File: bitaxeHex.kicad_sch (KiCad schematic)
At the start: 21 parts, among them J1 Screw Terminal, J2 Screw Terminal

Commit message: Move USB-C connector away from ESP32 to make room for chunky cables
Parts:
- J1, J2: footprint bitaxe:7770-screw-terminal -> bitaxe:7771-screw-terminal; DK 36-7770-ND -> 36-7771-ND; PARTNO 36-7770 -> 36-7771
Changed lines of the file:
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@@
       (effects (font (size 1.27 1.27)) hide)
     )
-    (property "Footprint" "bitaxe:7770-screw-terminal" (at 32.385 33.02 0)
+    (property "Footprint" "bitaxe:7771-screw-terminal" (at 32.385 33.02 0)
       (effects (font (size 1.27 1.27)) hide)
     )
@@
       (effects (font (size 1.27 1.27)) hide)
     )
-    (property "DK" "36-7770-ND" (at 32.385 33.02 0)
-      (effects (font (size 1.27 1.27)) hide)
-    )
-    (property "PARTNO" "36-7770" (at 32.385 33.02 0)
+    (property "DK" "36-7771-ND" (at 32.385 33.02 0)
+      (effects (font (size 1.27 1.27)) hide)
+    )
+    (property "PARTNO" "36-7771" (at 32.385 33.02 0)
       (effects (font (size 1.27 1.27)) hide)
     )
@@
       (effects (font (size 1.27 1.27)) hide)
     )
-    (property "Footprint" "bitaxe:7770-screw-terminal" (at 32.385 40.64 0)
-      (effects (font (size 1.27 1.27)) hide)
-    )
-    (property "Datasheet" "https://www.te.com/commerce/DocumentDelivery/DDEController?Action=srchrtrv&DocNm=63862&DocType=Customer+Drawing&DocLang=English" (at 32.385 40.64 0)
-      (effects (font (size 1.27 1.27)) hide)
-    )
-    (property "DK" "36-7770-ND" (at 32.385 40.64 0)
-      (effects (font (size 1.27 1.27)) hide)
-    )
-    (property "PARTNO" "36-7770" (at 32.385 40.64 0)
-      (effects (font (size 1.27 1.27)) hide)
-    )
+    (property "Footprint" "bitaxe:7771-screw-terminal" (at 32.385 40.64 0)
+      (effects (font (size 1.27 1.27)) hide)
+    )
+    (property "Datasheet" "https://mm.digikey.com/Volume0/opasdata/d220001/medias/docus/581/Metric_PCB_Screw_Terminals.pdf" (at 32.385 40.64 0)
+      (effects (font (size 1.27 1.27)) hide)
+    )
+    (property "DK" "36-7771-ND" (at 32.385 40.64 0)
+      (effects (font (size 1.27 1.27)) hide)
+    )
+    (property "PARTNO" "36-7771" (at 32.385 40.64 0)
+      (effects (font (size 1.27 1.27)) hide)
+    )

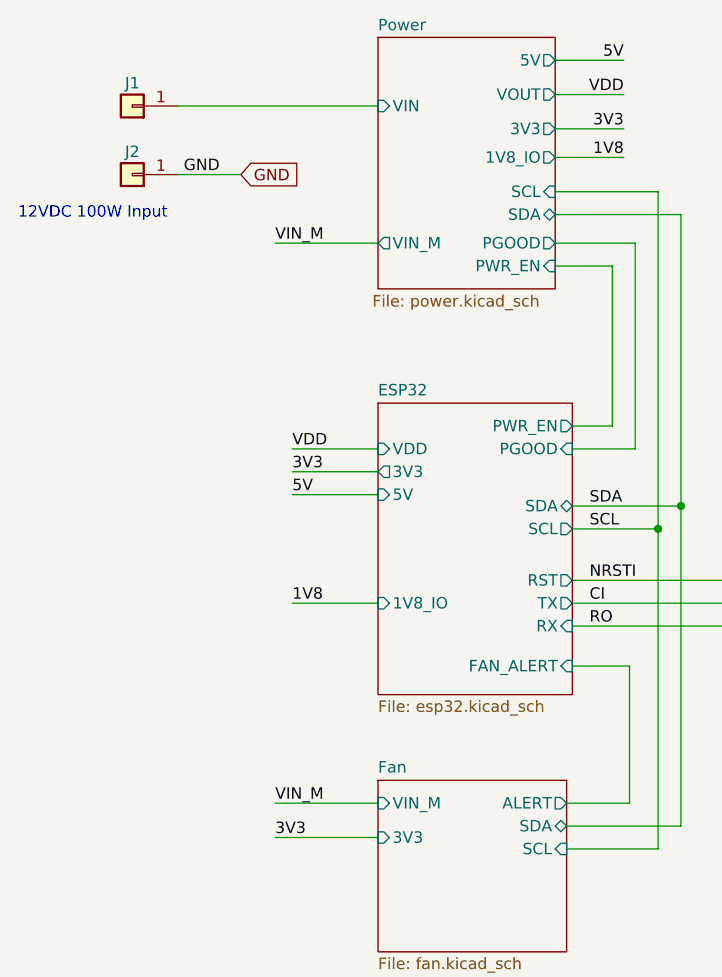
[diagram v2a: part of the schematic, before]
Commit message: remove INA219 power monitor
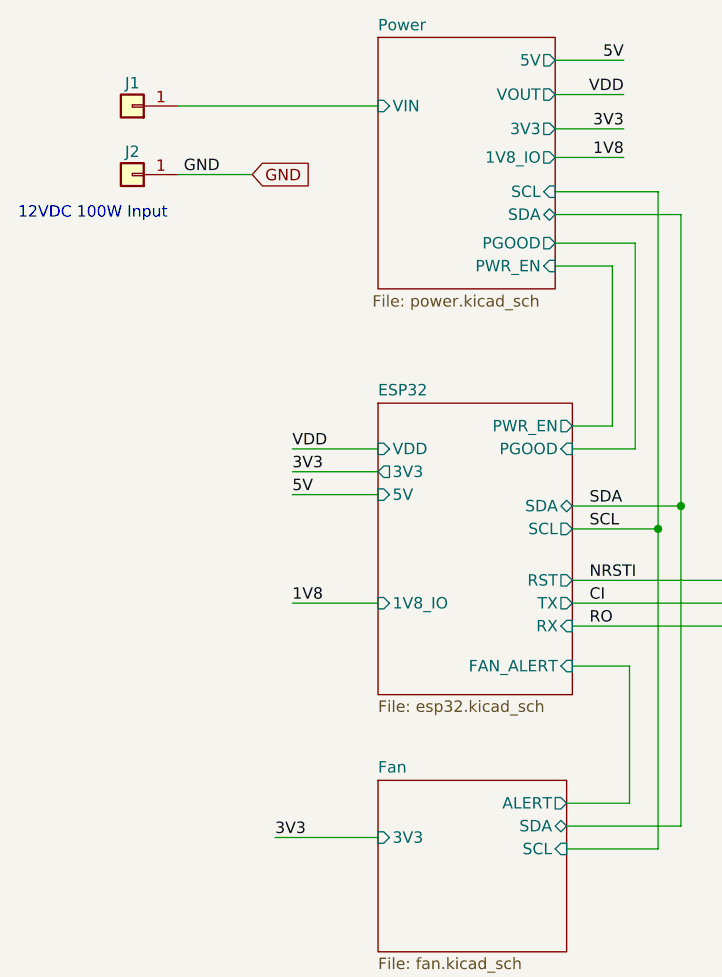
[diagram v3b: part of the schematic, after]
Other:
- sheet Fan ports: added none; removed VIN_M
- sheet Power ports: added none; removed VIN_M
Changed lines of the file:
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@@
-    (stroke (width 0) (type default))
-  )
-  (wire (pts (xy 48.26 110.49) (xy 59.69 110.49))
     (stroke (width 0) (type default))
   )
@@
     (stroke (width 0) (type default))
   )
-  (wire (pts (xy 37.465 40.64) (xy 44.45 40.64))
-    (stroke (width 0) (type default))
-  )
   (wire (pts (xy 200.66 76.2) (xy 191.77 76.2))
     (stroke (width 0) (type default))
@@
     (stroke (width 0) (type default))
   )
-  (wire (pts (xy 48.26 48.26) (xy 59.69 48.26))
-    (stroke (width 0) (type default))
-  )
   (wire (pts (xy 81.28 88.265) (xy 123.825 88.265))
     (stroke (width 0) (type default))
@@
   )
   (wire (pts (xy 93.345 113.03) (xy 93.345 77.47))
+    (stroke (width 0) (type default))
+  )
+  (wire (pts (xy 37.465 40.64) (xy 45.72 40.64))
     (stroke (width 0) (type default))
   )
@@
     (effects (font (size 1.27 1.27)) (justify left bottom))
   )
-  (label "VIN_M" (at 48.26 48.26 0) (fields_autoplaced)
-    (effects (font (size 1.27 1.27)) (justify left bottom))
-  )
   (label "GND" (at 106.68 114.935 0) (fields_autoplaced)
     (effects (font (size 1.27 1.27)) (justify left bottom))
@@
     (effects (font (size 1.27 1.27)) (justify left bottom))
   )
-  (label "VIN_M" (at 48.26 110.49 0) (fields_autoplaced)
-    (effects (font (size 1.27 1.27)) (justify left bottom))
-  )
   (label "SCL" (at 83.185 80.01 0) (fields_autoplaced)
     (effects (font (size 1.27 1.27)) (justify left bottom))
@@
     (effects (font (size 1.27 1.27)) (justify right bottom))
   )
-  (global_label "GND" (shape input) (at 44.45 40.64 0) (fields_autoplaced)
+  (global_label "GND" (shape input) (at 45.72 40.64 0) (fields_autoplaced)
     (effects (font (size 1.27 1.27)) (justify left))
-    (property "Intersheetrefs" "${INTERSHEET_REFS}" (at 50.7336 40.5606 0)
+    (property "Intersheetrefs" "${INTERSHEET_REFS}" (at 52.0036 40.5606 0)
       (effects (font (size 1.27 1.27)) (justify left) hide)
     )
@@
       (effects (font (size 1.27 1.27)) (justify right))
     )
-    (pin "VIN_M" input (at 59.69 110.49 180)
-      (effects (font (size 1.27 1.27)) (justify left))
-    )
     (instances
       (project "bitaxeHex"
@@
       (effects (font (size 1.27 1.27)) (justify right))
     )
-    (pin "VIN_M" output (at 59.69 48.26 180)
-      (effects (font (size 1.27 1.27)) (justify left))
-    )
-    (instances
+    (instances

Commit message: more routing
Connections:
- net Power/VIN renamed VIN
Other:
- sheet ESP32 ports: added SMB_ALRT; removed none
- sheet Fan ports: added 5V, VIN; removed none
- sheet Power ports: added GND, SMB_ALRT; removed none
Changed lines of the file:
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@@
+    (stroke (width 0) (type default))
+  )
+  (wire (pts (xy 96.52 40.005) (xy 79.375 40.005))
+    (stroke (width 0) (type default))
+  )
+  (wire (pts (xy 81.28 74.93) (xy 96.52 74.93))
     (stroke (width 0) (type default))
   )
@@
     (stroke (width 0) (type default))
   )
+  (wire (pts (xy 48.26 111.76) (xy 59.69 111.76))
+    (stroke (width 0) (type default))
+  )
   (wire (pts (xy 154.94 76.2) (xy 154.94 68.58))
     (stroke (width 0) (type default))
@@
     (stroke (width 0) (type default))
   )
-  (wire (pts (xy 79.375 38.735) (xy 86.995 38.735))
+  (wire (pts (xy 79.375 36.195) (xy 86.995 36.195))
+    (stroke (width 0) (type default))
+  )
+  (wire (pts (xy 48.895 48.895) (xy 59.69 48.895))
     (stroke (width 0) (type default))
   )
@@
     (stroke (width 0) (type default))
   )
+  (wire (pts (xy 96.52 74.93) (xy 96.52 40.005))
+    (stroke (width 0) (type default))
+  )
   (wire (pts (xy 179.07 90.805) (xy 200.66 90.805))
     (stroke (width 0) (type default))
@@
     (stroke (width 0) (type default))
   )
-  (wire (pts (xy 48.26 114.3) (xy 59.69 114.3))
+  (wire (pts (xy 48.26 116.84) (xy 59.69 116.84))
     (stroke (width 0) (type default))
   )
@@
     (stroke (width 0) (type default))
   )
+  (wire (pts (xy 48.26 123.19) (xy 59.69 123.19))
+    (stroke (width 0) (type default))
+  )
   (wire (pts (xy 154.94 99.06) (xy 161.29 99.06))
     (stroke (width 0) (type default))
@@
     (stroke (width 0) (type default))
   )
-  (wire (pts (xy 79.375 31.75) (xy 86.995 31.75))
+  (wire (pts (xy 79.375 29.21) (xy 86.995 29.21))
     (stroke (width 0) (type default))
   )
@@
     (stroke (width 0) (type default))
   )
-  (wire (pts (xy 79.375 27.94) (xy 86.995 27.94))
+  (wire (pts (xy 79.375 25.4) (xy 86.995 25.4))
     (stroke (width 0) (type default))
   )
@@
     (stroke (width 0) (type default))
   )
-  (wire (pts (xy 79.375 35.56) (xy 86.995 35.56))
+  (wire (pts (xy 79.375 33.02) (xy 86.995 33.02))
     (stroke (width 0) (type default))
   )
@@
     (effects (font (size 1.27 1.27)) (justify left bottom))
   )
+  (label "SMB_ALRT" (at 85.09 40.005 0) (fields_autoplaced)
+    (effects (font (size 1.27 1.27)) (justify left bottom))
+  )
   (label "1V8" (at 50.165 88.265 0) (fields_autoplaced)
     (effects (font (size 1.27 1.27)) (justify left bottom))
   )
-  (label "5V" (at 86.995 27.94 180) (fields_autoplaced)
+  (label "5V" (at 86.995 25.4 180) (fields_autoplaced)
     (effects (font (size 1.27 1.27)) (justify right bottom))
   )
@@
     (effects (font (size 1.27 1.27)) (justify right bottom))
   )
+  (label "5V" (at 48.26 123.19 0) (fields_autoplaced)
+    (effects (font (size 1.27 1.27)) (justify left bottom))
+  )
   (label "CI" (at 83.185 88.265 0) (fields_autoplaced)
     (effects (font (size 1.27 1.27)) (justify left bottom))
@@
     (effects (font (size 1.27 1.27)) (justify left bottom))
   )
-  (label "1V8" (at 86.995 38.735 180) (fields_autoplaced)
+  (label "1V8" (at 86.995 36.195 180) (fields_autoplaced)
     (effects (font (size 1.27 1.27)) (justify right bottom))
   )
-  (label "3V3" (at 86.995 35.56 180) (fields_autoplaced)
+  (label "VIN" (at 48.26 111.76 0) (fields_autoplaced)
+    (effects (font (size 1.27 1.27)) (justify left bottom))
+  )
+  (label "3V3" (at 86.995 33.02 180) (fields_autoplaced)
     (effects (font (size 1.27 1.27)) (justify right bottom))
   )
@@
     (effects (font (size 1.27 1.27)) (justify left bottom))
   )
-  (label "3V3" (at 48.26 114.3 0) (fields_autoplaced)
+  (label "3V3" (at 48.26 116.84 0) (fields_autoplaced)
     (effects (font (size 1.27 1.27)) (justify left bottom))
   )
@@
     (effects (font (size 1.27 1.27)) (justify left bottom))
   )
-  (label "VDD" (at 86.995 31.75 180) (fields_autoplaced)
+  (label "VDD" (at 86.995 29.21 180) (fields_autoplaced)
     (effects (font (size 1.27 1.27)) (justify right bottom))
+  )
+  (label "GND" (at 48.895 48.895 0) (fields_autoplaced)
+    (effects (font (size 1.27 1.27)) (justify left bottom))
+  )
+  (label "VIN" (at 47.625 33.02 0) (fields_autoplaced)
+    (effects (font (size 1.27 1.27)) (justify left bottom))
   )
   (global_label "GND" (shape input) (at 45.72 40.64 0) (fields_autoplaced)
@@
       (effects (font (size 1.27 1.27)) (justify right))
     )
-    (pin "3V3" input (at 59.69 114.3 180)
+    (pin "3V3" input (at 59.69 116.84 180)
       (effects (font (size 1.27 1.27)) (justify left))
     )
@@
       (effects (font (size 1.27 1.27)) (justify right))
     )
+    (pin "5V" input (at 59.69 123.19 180)
+      (effects (font (size 1.27 1.27)) (justify left))
+    )
+    (pin "VIN" input (at 59.69 111.76 180)
+      (effects (font (size 1.27 1.27)) (justify left))
+    )
     (instances
       (project "bitaxeHex"
@@
     )
   )
-  (sheet (at 59.69 25.4) (size 19.685 27.94)
+  (sheet (at 59.69 22.86) (size 19.685 30.48)
     (stroke (width 0.1524) (type solid))
     (fill (color 255 255 194 1.0000))
-    (property "Sheetname" "Power" (at 59.69 24.765 0)
+    (property "Sheetname" "Power" (at 59.69 22.225 0)
       (effects (font (size 1.27 1.27)) (justify left bottom))
     )
@@
       (effects (font (size 1.27 1.27)) (justify left top))
     )
-    (pin "VOUT" output (at 79.375 31.75 0)
+    (pin "VOUT" output (at 79.375 29.21 0)
       (effects (font (size 1.27 1.27)) (justify right))
     )
@@
       (effects (font (size 1.27 1.27)) (justify right))
     )
-    (pin "5V" output (at 79.375 27.94 0)
-      (effects (font (size 1.27 1.27)) (justify right))
-    )
-    (pin "3V3" output (at 79.375 35.56 0)
+    (pin "5V" output (at 79.375 25.4 0)
+      (effects (font (size 1.27 1.27)) (justify right))
+    )
+    (pin "3V3" output (at 79.375 33.02 0)
       (effects (font (size 1.27 1.27)) (justify right))
     )
@@
       (effects (font (size 1.27 1.27)) (justify right))
     )
-    (pin "1V8_IO" output (at 79.375 38.735 0)
+    (pin "1V8_IO" output (at 79.375 36.195 0)
       (effects (font (size 1.27 1.27)) (justify right))
     )
     (pin "PWR_EN" input (at 79.375 50.8 0)
+      (effects (font (size 1.27 1.27)) (justify right))
+    )
+    (pin "GND" input (at 59.69 48.895 180)
+      (effects (font (size 1.27 1.27)) (justify left))
+    )
+    (pin "SMB_ALRT" input (at 79.375 40.005 0)
       (effects (font (size 1.27 1.27)) (justify right))
     )
@@
       (effects (font (size 1.27 1.27)) (justify right))
     )
+    (pin "SMB_ALRT" input (at 81.28 74.93 0)
+      (effects (font (size 1.27 1.27)) (justify right))
+    )

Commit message: final polishing before gerbers
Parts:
- H3, H4: footprint MountingHole:MountingHole_3mm -> MountingHole:MountingHole_3mm_Pad_Via
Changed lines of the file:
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@@
       (effects (font (size 1.27 1.27)) (justify left))
     )
-    (property "Footprint" "MountingHole:MountingHole_3mm" (at 86.36 190.5 0)
+    (property "Footprint" "MountingHole:MountingHole_3mm_Pad_Via" (at 86.36 190.5 0)
       (effects (font (size 1.27 1.27)) hide)
     )
@@
       (effects (font (size 1.27 1.27)) (justify left))
     )
-    (property "Footprint" "MountingHole:MountingHole_3mm" (at 86.36 183.515 0)
+    (property "Footprint" "MountingHole:MountingHole_3mm_Pad_Via" (at 86.36 183.515 0)
       (effects (font (size 1.27 1.27)) hide)
     )

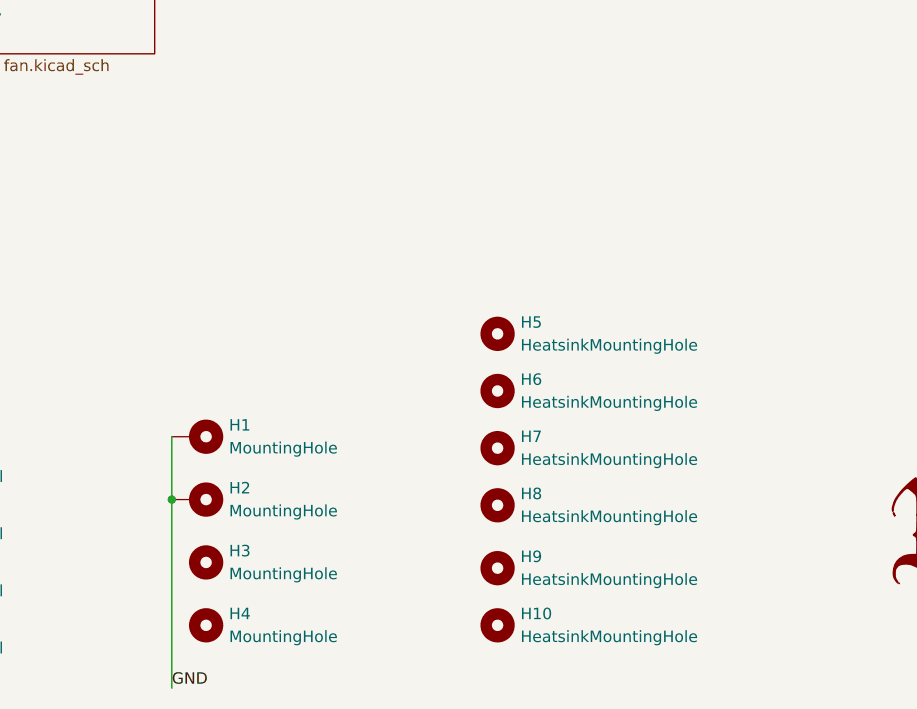
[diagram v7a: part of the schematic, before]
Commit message: Add mounting holes, remove some caps and power resistors
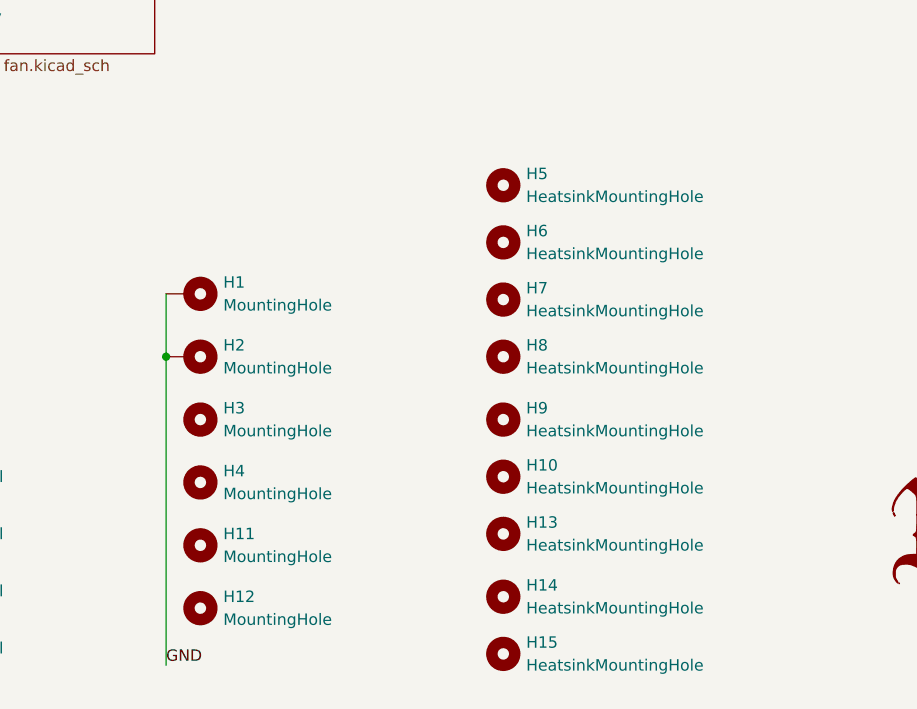
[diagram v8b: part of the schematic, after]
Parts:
- added H11, H12: MountingHole, MountingHole:MountingHole_3mm_Pad_Via, symbol Mechanical:MountingHole
- added H13, H14, H15: HeatsinkMountingHole, bitaxe:2.2mm_mounting, symbol Mechanical:MountingHole
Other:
- moved on the sheet: H1, H10, H2, H3, H4, H5, H6, H7, H8, H9
